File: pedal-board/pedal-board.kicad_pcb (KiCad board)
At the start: 2 copper layers, 168 x 64 mm, 57 parts, among them J1 AudioJack0, J10 CH7, J11 CH7, J12 Qwiic, J2 AudioJack1, J3 AudioJack2, J4 AudioJack3, J5 Qwiic, J6 CH7, J7 CH7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

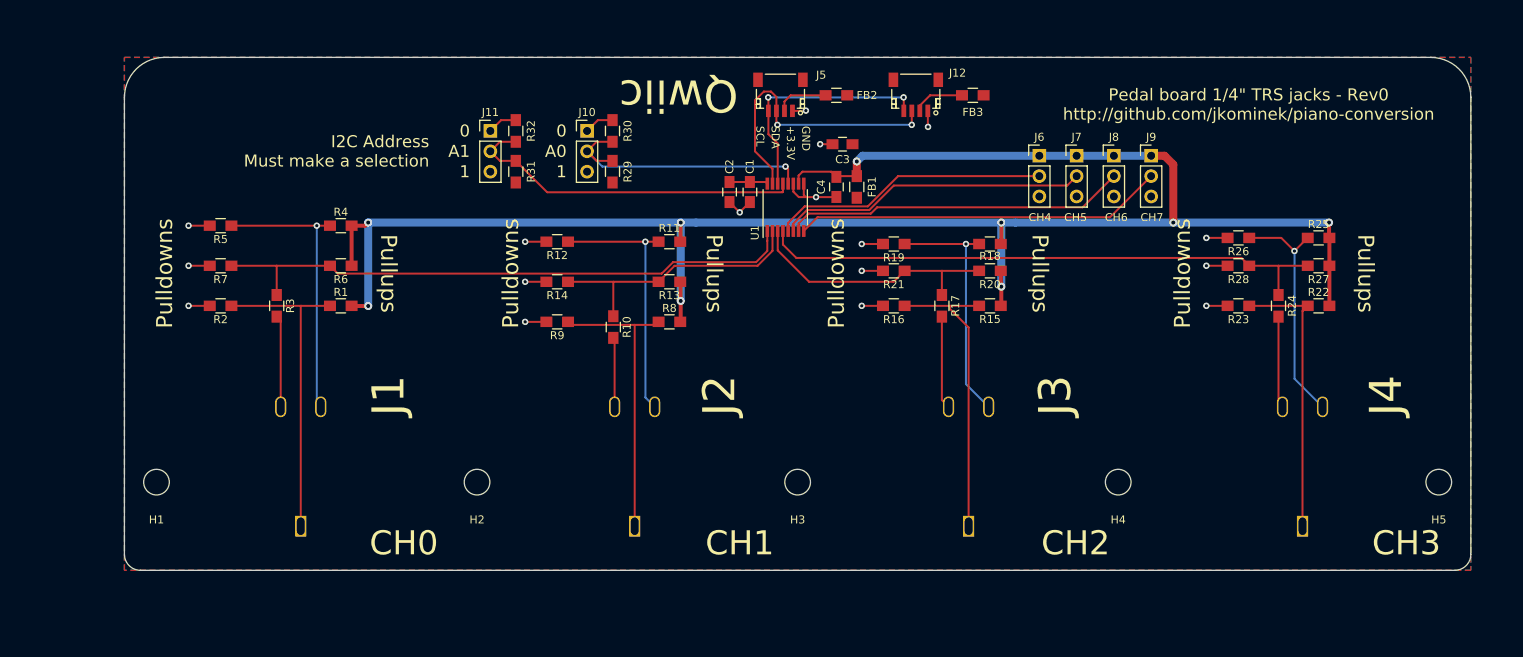
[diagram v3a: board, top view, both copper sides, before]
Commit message: Rev 1 first batch of changes
- Made it narrower, but had to expand the space between mounting holes.
- Moved the jacks back 2.3mm.
- 10mm to board edge, 5mm clearance on the inside of the board, 7.5mm clearance on either side
- Fixed the outline to be silkscreen, not a hole in the mask
- Added I2C bus header
- Made nice little three pad footprints for spots where you need a pull up or a pull down.
- Drastically increased the space between the Qwiic headers
- On the pedal jacks, the signal is really on the Tip, not the ring where I had it. Not sure what I was thinking.
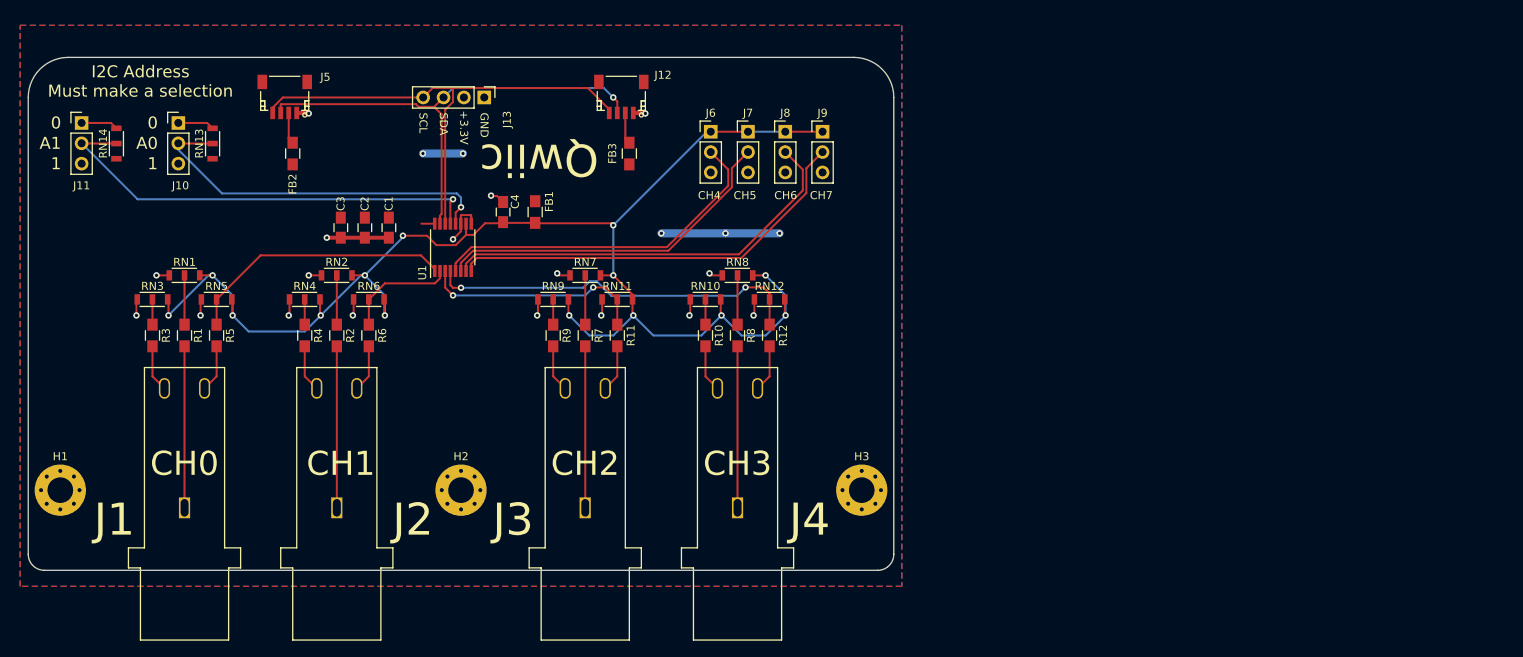
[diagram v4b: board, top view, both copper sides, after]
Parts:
- removed H4, H5: MountingHole, Mounting_Holes:MountingHole_3.2mm_M3
- removed R13, R14, R15, R16, R18, R19, R20, R21, R22, R23, R25, R26, R27, R28: XXX, Resistors_SMD:R_0805_HandSoldering
- removed R17, R24: 10, Resistors_SMD:R_0805_HandSoldering
- removed R29, R30, R31, R32: DNP, Resistors_SMD:R_0805_HandSoldering
- added J13: Qwiic, Pin_Headers:Pin_Header_Straight_1x04_Pitch2.54mm, F.Cu at (72.9, 39.0)
- added RN1: Div, footprints:R_0805_Divider, F.Cu at (35.5, 61.2)
- added RN10: Div, footprints:R_0805_Divider, F.Cu at (100.5, 64.2)
- added RN11: Div, footprints:R_0805_Divider, F.Cu at (89.5, 64.2)
- added RN12: Div, footprints:R_0805_Divider, F.Cu at (108.5, 64.2)
- added RN13: Div, footprints:R_0805_Divider, F.Cu at (39.0, 44.8)
- added RN14: Div, footprints:R_0805_Divider, F.Cu at (27.0, 44.8)
- added RN2: Div, footprints:R_0805_Divider, F.Cu at (54.5, 61.2)
- added RN3: Div, footprints:R_0805_Divider, F.Cu at (31.5, 64.2)
- added RN4: Div, footprints:R_0805_Divider, F.Cu at (50.5, 64.2)
- added RN5: Div, footprints:R_0805_Divider, F.Cu at (39.5, 64.2)
- added RN6: Div, footprints:R_0805_Divider, F.Cu at (58.5, 64.2)
- added RN7: Div, footprints:R_0805_Divider, F.Cu at (85.5, 61.2)
- added RN8: Div, footprints:R_0805_Divider, F.Cu at (104.5, 61.2)
- added RN9: Div, footprints:R_0805_Divider, F.Cu at (81.5, 64.2)
- H1, H2, H3: value MountingHole -> MountingHole_Pad; footprint Mounting_Holes:MountingHole_3.2mm_M3 -> Mounting_Holes:MountingHole_3.2mm_M3_Pad_Via
- R1, R11, R12, R2, R4, R5, R6, R7, R8, R9: value XXX -> 10
- moved J4 70.5 mm to (104.5, 97.7)
- moved FB2 68.2 mm to (49.0, 46.0), turned to 90 degrees
- moved C3 63.5 mm to (55.0, 55.2), turned to 270 degrees
- moved J5 61.9 mm to (48.0, 39.0)
- moved J11 51.0 mm to (22.7, 42.2)
- moved J10 51.0 mm to (34.7, 42.2)
- moved J3 47.9 mm to (85.5, 97.7)
- moved R7 46.3 mm to (85.5, 68.7), turned to 270 degrees
- moved C2 45.7 mm to (58.0, 55.2)
- moved C1 45.3 mm to (61.0, 55.2)
- moved FB3 43.5 mm to (91.0, 46.0), turned to 90 degrees
- moved U1 41.8 mm to (69.0, 57.7)
- moved C4 41.7 mm to (75.2, 53.3), turned to 90 degrees
- moved J9 41.1 mm to (115.1, 43.3)
- moved J6 41.1 mm to (101.2, 43.3)
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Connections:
- H1 pad 1: (no net) -> GND
- H2 pad 1: (no net) -> GND
- H3 pad 1: (no net) -> GND
- R1 pad 1: Net-(J1-PadS) -> Net-(R1-Pad1)
- R1 pad 2: +3.3VA -> Net-(J1-PadS)
- R10 pad 1: /CH1 -> Net-(R10-Pad1)
- R10 pad 2: Net-(J2-PadR) -> Net-(J4-PadR)
- R11 pad 1: Net-(J2-PadT) -> /CH2
- R11 pad 2: +3.3VA -> Net-(J3-PadT)
- R12 pad 1: Net-(J2-PadT) -> /CH3
- R12 pad 2: GND -> Net-(J4-PadT)
- R2 pad 1: Net-(J1-PadS) -> Net-(R2-Pad1)
- R2 pad 2: GND -> Net-(J2-PadS)
- R3 pad 1: /CH0 -> Net-(R3-Pad1)
- R4 pad 1: Net-(J1-PadT) -> Net-(R4-Pad1)
- R4 pad 2: +3.3VA -> Net-(J2-PadR)
- R5 pad 1: Net-(J1-PadT) -> /CH0
- R5 pad 2: GND -> Net-(J1-PadT)
- R6 pad 1: +3.3VA -> /CH1
- R6 pad 2: /CH0 -> Net-(J2-PadT)
- R7 pad 1: /CH0 -> Net-(R7-Pad1)
- R7 pad 2: GND -> Net-(J3-PadS)
- R8 pad 1: Net-(J2-PadS) -> Net-(R8-Pad1)
- R8 pad 2: +3.3VA -> Net-(J4-PadS)
- R9 pad 1: Net-(J2-PadS) -> Net-(R9-Pad1)
- R9 pad 2: GND -> Net-(J3-PadR)
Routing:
- net +3.3VA: track 240.5 -> 179.6 mm, vias 9 -> 14
- net /CH0: track 74.6 -> 33.6 mm
- net /SCL: track 29.8 -> 62.6 mm, vias 2 -> 0
- net Net-(J1-PadT): track 35.1 -> 5.87 mm, vias 1 -> 0
- net Net-(J2-PadT): track 32.4 -> 5.87 mm, vias 1 -> 0
- net Net-(J3-PadT): track 30.8 -> 5.87 mm, vias 1 -> 0
- net /SDA: track 36.7 -> 61.3 mm, vias 2 -> 1
- net /CH3: track 71.9 -> 47.5 mm, vias 0 -> 2
- net Net-(J4-PadT): track 29.5 -> 5.87 mm, vias 1 -> 0
- net /CH1: track 33.9 -> 14.0 mm
- net Net-(J1-PadS): track 39.8 -> 20.2 mm
- net Net-(J3-PadS): track 37.8 -> 20.2 mm
- net +3V3: track 4.79 -> 21.4 mm, vias 0 -> 5
- net Net-(J2-PadS): track 36.8 -> 20.2 mm
- net Net-(J4-PadS): track 35.1 -> 20.2 mm
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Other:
- board size 168 x 64 mm -> 108 x 64 mm
- board text removed: "Pulldowns"
- board text removed: "Pullups"

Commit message: Tweak some traces, and bump the board rev
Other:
- board text added: "3V3"
- board text added: "JLCJLCJLCJLC"
- board text added: "Pedal board 1/4" TRS jacks - Rev1 http://github.com/jkominek/piano-conversion"
- board text removed: "+3.3V"
- board text removed: "Pedal board 1/4" TRS jacks - Rev0 http://github.com/jkominek/piano-conversion"
